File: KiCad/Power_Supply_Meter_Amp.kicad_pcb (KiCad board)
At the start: 4 copper layers, 150 x 85.2 mm, 95 parts, among them J33 Pegel_In, J34 VU_Meter_Out, J35 Pegel_In, J36 Pegel_In, J37 LED_Out, J39 VCC_IN, J40 Conn_02x07_Odd_Even, J41 Conn_02x07_Odd_Even, J42 Pegel_In, J43 VCC_OUT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

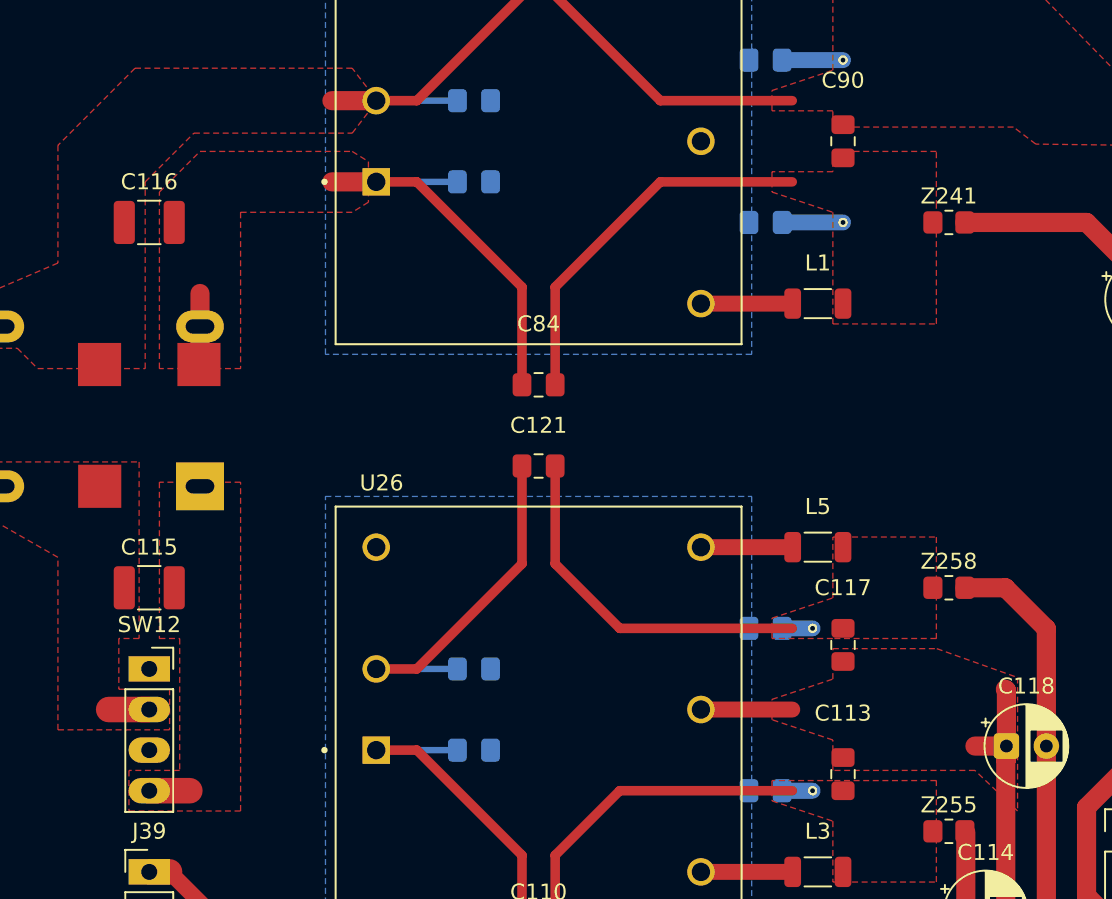
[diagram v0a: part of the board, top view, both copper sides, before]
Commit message: Output phasen korrektur durch invertierender verstärker
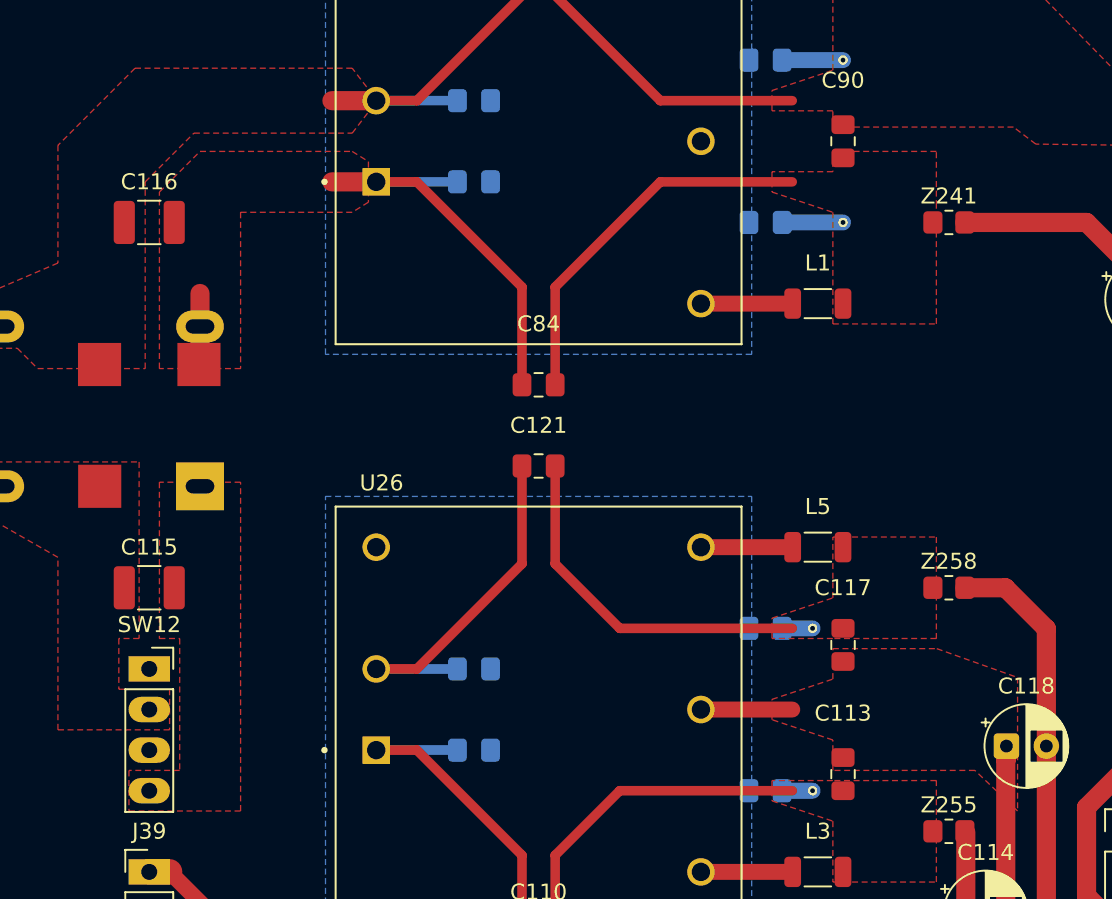
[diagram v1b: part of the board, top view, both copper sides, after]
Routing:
- net GND_P: track 34.6 -> 28.2 mm
- net Net-(C115-Pad1): track 2.79 -> 0.25 mm
- net Net-(C115-Pad2): track 2.79 -> 0.25 mm
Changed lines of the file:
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@@
 		(start 70.0825 67.31)
 		(end 65.0025 67.31)
-		(width 0.4)
+		(width 0.6)
 		(layer "B.Cu")
 		(net 4)
@@
 		(start 70.0825 102.87)
 		(end 65.0025 102.87)
-		(width 0.4)
+		(width 0.6)
 		(layer "B.Cu")
 		(net 4)
@@
 		(start 70.0825 62.23)
 		(end 65.0025 62.23)
-		(width 0.4)
+		(width 0.6)
 		(layer "B.Cu")
 		(net 7)
@@
 		(start 70.0825 97.79)
 		(end 65.0025 97.79)
-		(width 0.4)
+		(width 0.6)
 		(layer "B.Cu")
 		(net 7)
@@
 	(segment
 		(start 50.8 100.33)
-		(end 48.26 100.33)
-		(width 1.6)
-		(layer "F.Cu")
-		(net 9)
-	)
-	(segment
-		(start 50.8 100.33)
 		(end 50.546 100.33)
 		(width 0.4)
@@
 	)
 	(segment
-		(start 104.437388 102.616)
-		(end 102.4675 102.616)
-		(width 1.2)
-		(layer "F.Cu")
-		(net 49)
-	)
-	(segment
 		(start 104.397388 113.689888)
 		(end 104.397388 115.827388)
@@
 	)
 	(segment
-		(start 104.437388 103.440112)
-		(end 104.437388 100.965)
-		(width 1.2)
-		(layer "F.Cu")
-		(net 49)
-	)
-	(segment
 		(start 104.397388 112.395)
 		(end 104.397388 103.480112)
@@
 	)
 	(segment
-		(start 104.437388 99.124888)
-		(end 104.437388 100.965)
-		(width 1.2)
-		(layer "F.Cu")
-		(net 49)
-	)
-	(segment
 		(start 104.397388 115.827388)
 		(end 107.95 119.38)
@@
 		(start 104.397388 112.395)
 		(end 104.397388 113.689888)
-		(width 1.2)
-		(layer "F.Cu")
-		(net 49)
-	)
-	(segment
-		(start 104.437388 99.124888)
-		(end 104.3725 99.06)
 		(width 1.2)
 		(layer "F.Cu")
@@
 	(segment
 		(start 50.8 105.41)
-		(end 53.34 105.41)
-		(width 1.6)
-		(layer "F.Cu")
-		(net 59)
-	)
-	(segment
-		(start 50.8 105.41)
 		(end 51.054 105.41)
 		(width 0.4)
@@
 		(hatch edge 0.5)
 		(priority 3)
-		(connect_pads
+		(connect_pads yes
 			(clearance 0.5)
 		)
@@
 		(hatch edge 0.5)
 		(priority 5)
-		(connect_pads
+		(connect_pads yes
 			(clearance 0.5)
 		)
@@
 		(hatch edge 0.5)
 		(priority 1)
-		(connect_pads
+		(connect_pads yes
 			(clearance 0.5)
 		)
@@
 		(hatch edge 0.5)
 		(priority 5)
-		(connect_pads
+		(connect_pads yes
 			(clearance 0.5)
 		)
@@
 		(hatch edge 0.5)
 		(priority 5)
-		(connect_pads
+		(connect_pads yes
 			(clearance 0.5)
 		)
@@
 		(hatch edge 0.5)
 		(priority 4)
-		(connect_pads
+		(connect_pads yes
 			(clearance 0.5)
 		)
@@
 		(hatch edge 0.5)
 		(priority 5)
-		(connect_pads
+		(connect_pads yes
 			(clearance 0.5)
 		)
@@
 		(hatch edge 0.5)
 		(priority 2)
-		(connect_pads
+		(connect_pads yes
 			(clearance 0.5)
 		)
@@
 		(hatch edge 0.5)
 		(priority 6)
-		(connect_pads
+		(connect_pads yes
 			(clearance 0.5)
 		)
@@
 		(layer "B.Cu")
 		(hatch edge 0.5)
-		(connect_pads
+		(connect_pads yes
 			(clearance 0.5)
 		)
@@
 		(layer "B.Cu")
 		(hatch edge 0.5)
-		(connect_pads
-			(clearance 0.5)
-		)
+		(connect_pads yes
+			(clearance 0.5)
+		)

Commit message: DRC Update
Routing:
- net Net-(U25-+VIN): track 92.5 -> 90.4 mm
- net GND_M: vias 21 -> 22
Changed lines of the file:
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@@
 	(generator_version "9.0")
 	(general
-		(thickness 1.635)
+		(thickness 2.003)
 		(legacy_teardrops no)
 	)
@@
 			(layer "F.Mask"
 				(type "Top Solder Mask")
-				(thickness 0.01)
+				(thickness 0.03)
 			)
 			(layer "F.Cu"
@@
 			(layer "dielectric 1"
 				(type "prepreg")
-				(thickness 0.1)
-				(material "FR4")
-				(epsilon_r 4.5)
-				(loss_tangent 0.02) addsublayer
-				(thickness 0)
+				(thickness 0.107)
+				(material "3313*1")
+				(epsilon_r 4.1)
+				(loss_tangent 0) addsublayer
+				(thickness 0.0535)
+				(material "1080*1")
+				(epsilon_r 3.91)
+				(loss_tangent 0)
 			)
 			(layer "In1.Cu"
 				(type "copper")
-				(thickness 0.035)
+				(thickness 0.061)
 			)
 			(layer "dielectric 2"
-				(type "core")
-				(thickness 1.24)
-				(material "FR4")
-				(epsilon_r 4.5)
-				(loss_tangent 0.02)
+				(type "prepreg")
+				(thickness 1.36)
+				(material "Core")
+				(epsilon_r 4.6)
+				(loss_tangent 0)
 			)
 			(layer "In2.Cu"
 				(type "copper")
-				(thickness 0.035)
+				(thickness 0.061)
 			)
 			(layer "dielectric 3"
 				(type "prepreg")
-				(thickness 0.1)
-				(material "FR4")
-				(epsilon_r 4.5)
-				(loss_tangent 0.02)
+				(thickness 0.0535)
+				(material "1080*1")
+				(epsilon_r 3.91)
+				(loss_tangent 0) addsublayer
+				(thickness 0.107)
+				(material "3313*1")
+				(epsilon_r 4.1)
+				(loss_tangent 0)
 			)
 			(layer "B.Cu"
 				(type "copper")
-				(thickness 0.035)
+				(thickness 0.07)
 			)
 			(layer "B.Mask"
 				(type "Bottom Solder Mask")
-				(thickness 0.01)
+				(thickness 0.03)
 			)
 			(layer "B.Paste"
@@
 	)
 	(segment
-		(start 53.975 74.295)
-		(end 53.975 76.36)
-		(width 1.2)
-		(layer "F.Cu")
-		(net 4)
-	)
-	(segment
 		(start 67.5425 67.31)
 		(end 65.0025 67.31)
@@
 	(via
 		(at 94.2125 69.85)
-		(size 0.6)
+		(size 0.7)
 		(drill 0.3)
 		(layers "F.Cu" "B.Cu")
@@
 	(via
 		(at 92.3075 105.41)
-		(size 0.6)
+		(size 0.7)
 		(drill 0.3)
 		(layers "F.Cu" "B.Cu")
@@
 	(via
 		(at 92.3075 95.25)
-		(size 0.6)
+		(size 0.7)
 		(drill 0.3)
 		(layers "F.Cu" "B.Cu")
@@
 	(via
 		(at 94.2125 59.69)
-		(size 0.6)
+		(size 0.7)
 		(drill 0.3)
 		(layers "F.Cu" "B.Cu")
@@
 	(via
 		(at 166.835 115.4)
-		(size 0.6)
+		(size 0.7)
 		(drill 0.3)
 		(layers "F.Cu" "B.Cu")
@@
 	(via
 		(at 149.309 97.62)
-		(size 0.6)
+		(size 0.7)
 		(drill 0.3)
 		(layers "F.Cu" "B.Cu")
@@
 	(via
 		(at 154.135 92.54)
-		(size 0.6)
+		(size 0.7)
 		(drill 0.3)
 		(layers "F.Cu" "B.Cu")
@@
 	(via
 		(at 166.835 97.62)
-		(size 0.6)
+		(size 0.7)
 		(drill 0.3)
 		(layers "F.Cu" "B.Cu")
@@
 	(via
 		(at 170.18 73.66)
-		(size 0.6)
+		(size 0.7)
 		(drill 0.3)
 		(layers "F.Cu" "B.Cu")
@@
 	(via
 		(at 149.309 72.22)
-		(size 0.6)
+		(size 0.7)
 		(drill 0.3)
 		(layers "F.Cu" "B.Cu")
@@
 	(via
 		(at 149.309 102.7)
-		(size 0.6)
+		(size 0.7)
 		(drill 0.3)
 		(layers "F.Cu" "B.Cu")
@@
 	(via
 		(at 170.661 102.7)
-		(size 0.6)
+		(size 0.7)
 		(drill 0.3)
 		(layers "F.Cu" "B.Cu")
@@
 	(via
 		(at 165.1 49.53)
-		(size 1.2)
-		(drill 0.6)
+		(size 0.7)
+		(drill 0.3)
 		(layers "F.Cu" "B.Cu")
 		(free yes)
@@
 	(via
 		(at 173.185 95.08)
-		(size 0.6)
+		(size 0.7)
 		(drill 0.3)
 		(layers "F.Cu" "B.Cu")
@@
 	(via
 		(at 157.31 116.67)
-		(size 0.6)
+		(size 0.7)
 		(drill 0.3)
 		(layers "F.Cu" "B.Cu")
@@
 	(via
 		(at 173.82 120.48)
-		(size 0.6)
+		(size 0.7)
 		(drill 0.3)
 		(layers "F.Cu" "B.Cu")
@@
 	(via
 		(at 154.135 64.6)
-		(size 0.6)
+		(size 0.7)
 		(drill 0.3)
 		(layers "F.Cu" "B.Cu")
@@
 	)
 	(via
+		(at 165.1 50.8)
+		(size 0.7)
+		(drill 0.3)
+		(layers "F.Cu" "B.Cu")
+		(free yes)
+		(net 51)
+	)
+	(via
 		(at 154.135 79.84)
-		(size 0.6)
+		(size 0.7)
 		(drill 0.3)
 		(layers "F.Cu" "B.Cu")
@@
 	(via
 		(at 154.135 107.78)
-		(size 0.6)
+		(size 0.7)
 		(drill 0.3)
 		(layers "F.Cu" "B.Cu")
@@
 	(via
 		(at 149.309 74.76)
-		(size 0.6)
+		(size 0.7)
 		(drill 0.3)
 		(layers "F.Cu" "B.Cu")
@@
 	(via
 		(at 155.405 110.32)
-		(size 0.6)
+		(size 0.7)
 		(drill 0.3)
 		(layers "F.Cu" "B.Cu")
@@
 	(via
 		(at 149.309 69.68)
-		(size 0.6)
+		(size 0.7)
 		(drill 0.3)
 		(layers "F.Cu" "B.Cu")
@@
 	(via
 		(at 149.309 100.16)
-		(size 0.6)
+		(size 0.7)
 		(drill 0.3)
 		(layers "F.Cu" "B.Cu")
@@
 	(via
 		(at 149.055 84.92)
-		(size 0.6)
+		(size 0.7)
 		(drill 0.3)
 		(layers "F.Cu" "B.Cu")
@@
 	(via
 		(at 165.1 52.07)
-		(size 1.2)
-		(drill 0.6)
+		(size 0.7)
+		(drill 0.3)
 		(layers "F.Cu" "B.Cu")
 		(free yes)
@@
 	(via
 		(at 178.9 110.32)
-		(size 0.6)
+		(size 0.7)
 		(drill 0.3)
 		(layers "F.Cu" "B.Cu")

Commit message: Gerber Update
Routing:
- net GND_M: track 32.2 -> 28.9 mm
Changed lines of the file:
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@@
 	)
 	(layers
-		(0 "F.Cu" signal "Signal")
-		(4 "In1.Cu" jumper "GND")
-		(6 "In2.Cu" power "Versorgungslagen")
-		(2 "B.Cu" power "Überbrückung")
+		(0 "F.Cu" signal "Signal.F.Cu")
+		(4 "In1.Cu" jumper "GND.1.Cu")
+		(6 "In2.Cu" power "Versorgungslagen.2.Cu")
+		(2 "B.Cu" power "Überbrückung.B.Cu")
 		(9 "F.Adhes" user "F.Adhesive")
 		(11 "B.Adhes" user "B.Adhesive")
@@
 			(plot_on_all_layers_selection 0x00000000_00000000_00000000_00000000)
 			(disableapertmacros no)
-			(usegerberextensions no)
+			(usegerberextensions yes)
 			(usegerberattributes yes)
 			(usegerberadvancedattributes yes)
-			(creategerberjobfile yes)
+			(creategerberjobfile no)
 			(dashed_line_dash_ratio 12.000000)
 			(dashed_line_gap_ratio 3.000000)
@@
 			(outputformat 1)
 			(mirror no)
-			(drillshape 1)
+			(drillshape 0)
 			(scaleselection 1)
-			(outputdirectory "")
+			(outputdirectory "Gerber/Power_PCB/")
 		)
 	)
@@
 	)
 	(segment
-		(start 173.82 120.48)
-		(end 174.725 120.48)
-		(width 0.6)
-		(layer "F.Cu")
-		(net 51)
-	)
-	(segment
 		(start 172.55 95.08)
 		(end 173.185 95.08)
@@
 	)
 	(segment
-		(start 168.105 115.4)
-		(end 166.835 115.4)
-		(width 1)
-		(layer "F.Cu")
-		(net 51)
-	)
-	(segment
 		(start 172.55 98.89)
 		(end 172.55 95.08)
@@
 	)
 	(segment
-		(start 170.18 73.66)
-		(end 170.18 74.76)
-		(width 1)
-		(layer "F.Cu")
-		(net 51)
-	)
-	(segment
 		(start 168.105 97.62)
 		(end 166.835 97.62)
@@
 	)
 	(via
-		(at 166.835 115.4)
+		(at 168.105 115.4)
 		(size 0.7)
 		(drill 0.3)
@@
 	)
 	(via
-		(at 170.18 73.66)
+		(at 170.18 74.76)
 		(size 0.7)
 		(drill 0.3)
@@
 	)
 	(via
-		(at 173.82 120.48)
+		(at 174.725 120.48)
 		(size 0.7)
 		(drill 0.3)

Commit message: Gerber Update
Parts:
- moved C101 2.54 mm to (175.7, 97.6)
- moved C110 2.54 mm to (75.2, 118.1)
- moved C111 2.54 mm to (89.4, 108.0)
- moved C115 2.54 mm to (50.8, 95.2)
- moved C116 2.54 mm to (50.8, 72.4)
- moved C117 2.54 mm to (94.2, 98.8)
- moved C118 2.54 mm to (104.4, 105.2)
- moved C120 2.54 mm to (89.4, 97.8)
- moved C85 2.54 mm to (171.1, 53.3)
- moved C86 2.54 mm to (89.4, 72.4)
- moved C87 2.54 mm to (151.8, 74.8)
- moved C88 2.54 mm to (151.8, 102.7)
- moved C90 2.54 mm to (94.2, 67.3)
- moved C93 2.54 mm to (169.1, 102.7)
- moved D1 2.54 mm to (169.1, 67.1)
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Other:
- board size 150 x 85.2 mm -> 150 x 90 mm
- board text added: "Energieversorgung"
- board text added: "Pegelanzeige"
